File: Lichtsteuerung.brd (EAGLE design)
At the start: 157.7 x 86.4 mm, 136 parts, among them IC1 74HC595D, IC10 TSR_1-2450, IC11 MEGA64-A, IC12 75176AD, IC13 DS1307SO8, IC2 74HC595D, IC3 74HC595D, IC4 74HC595D, IC5 75176AD, IC6 MEGA8-AI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

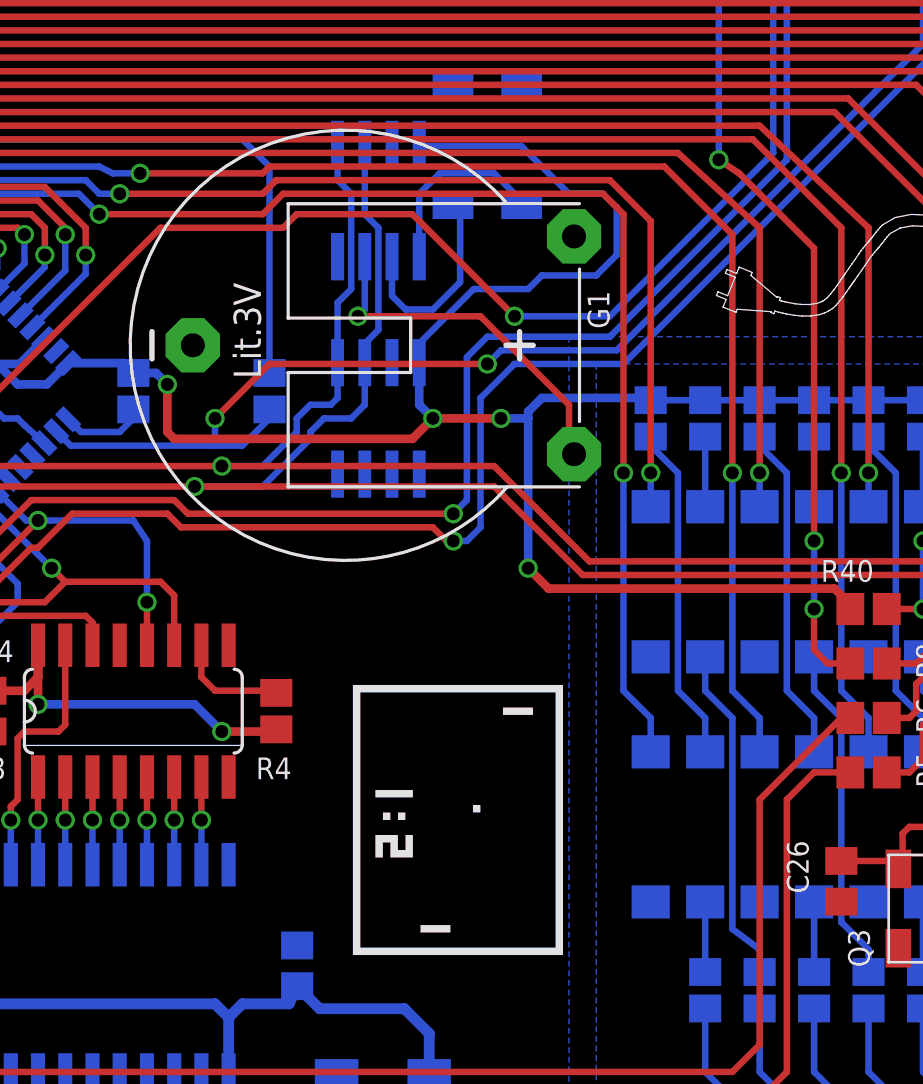
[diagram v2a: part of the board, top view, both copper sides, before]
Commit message: Fixed wrong battery holder
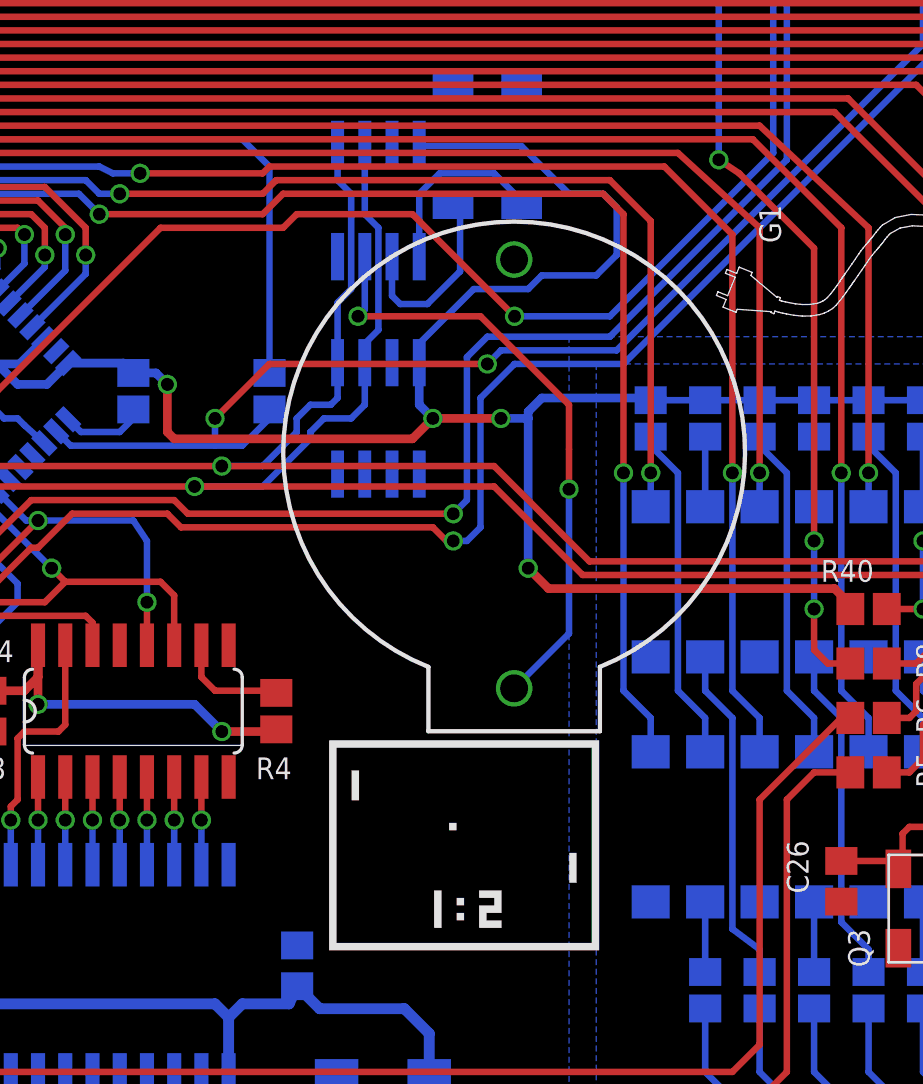
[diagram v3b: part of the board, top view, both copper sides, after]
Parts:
- G1: value CR2032H -> (none); device battery:CR2032H -> SparkFun:BATTCOM_20MM_PTH
- moved G1 8.94 mm to (104.1, 56.9)
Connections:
- net GND: now also G1.2; no longer G1.-
- net N$40: now also G1.1; no longer G1.+
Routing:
- net N$40: track 16.9 -> 28.8 mm, vias 1 -> 2
- net N$42: track 9.51 -> 9.01 mm
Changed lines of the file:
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@@
 <setting verticaltext="up"/>
 </settings>
-<grid distance="39.3700787" unitdist="mil" unit="mil" style="lines" multiple="1" display="yes" altdistance="0.5" altunitdist="mm" altunit="mm"/>
+<grid distance="0.254" unitdist="mm" unit="mm" style="lines" multiple="5" display="yes" altdistance="1.27" altunitdist="mm" altunit="mm"/>
 <layers>
 <layer number="1" name="Top" color="4" fill="1" visible="yes" active="yes"/>
@@
 <text x="7.7" y="4.2" size="1.016" layer="25" rot="R90">Digital Outputs</text>
 <text x="60.9" y="4.2" size="1.016" layer="25" rot="R90">Digital Outputs</text>
-<rectangle x1="100.275" y1="25.025" x2="100.625" y2="26.425" layer="25" rot="R90"/>
-<rectangle x1="104.125" y1="35.175" x2="104.475" y2="36.575" layer="25" rot="R90"/>
-<rectangle x1="102.2" y1="31.15" x2="102.55" y2="31.5" layer="25" rot="R90"/>
-<rectangle x1="97.3" y1="29.4" x2="98.35" y2="29.75" layer="25" rot="R90"/>
-<rectangle x1="98.175" y1="29.575" x2="98.525" y2="30.275" layer="25" rot="R90"/>
-<rectangle x1="98.175" y1="29.225" x2="98.875" y2="29.575" layer="25" rot="R90"/>
-<rectangle x1="98.875" y1="28.875" x2="99.225" y2="29.575" layer="25" rot="R90"/>
-<rectangle x1="98.875" y1="29.575" x2="99.575" y2="29.925" layer="25" rot="R90"/>
-<rectangle x1="98" y1="30.8" x2="98.35" y2="31.15" layer="25" rot="R90"/>
-<rectangle x1="98.7" y1="30.8" x2="99.05" y2="31.15" layer="25" rot="R90"/>
-<rectangle x1="98.35" y1="31.15" x2="98.7" y2="32.9" layer="25" rot="R90"/>
-<rectangle x1="90.825" y1="30.625" x2="102.725" y2="30.975" layer="25" rot="R90"/>
-<rectangle x1="99.925" y1="30.625" x2="112.525" y2="30.975" layer="25" rot="R90"/>
-<rectangle x1="101.15" y1="19.95" x2="101.5" y2="29.4" layer="25" rot="R90"/>
-<rectangle x1="101.15" y1="32.2" x2="101.5" y2="41.65" layer="25" rot="R90"/>
+<rectangle x1="106.688" y1="27.868" x2="107.038" y2="29.268" layer="25" rot="R180"/>
+<rectangle x1="96.538" y1="31.718" x2="96.888" y2="33.118" layer="25" rot="R180"/>
+<rectangle x1="101.088" y1="30.318" x2="101.438" y2="30.668" layer="25" rot="R180"/>
+<rectangle x1="102.488" y1="25.768" x2="103.538" y2="26.118" layer="25" rot="R180"/>
+<rectangle x1="102.488" y1="26.118" x2="102.838" y2="26.818" layer="25" rot="R180"/>
+<rectangle x1="102.838" y1="26.468" x2="103.538" y2="26.818" layer="25" rot="R180"/>
+<rectangle x1="103.188" y1="26.818" x2="103.538" y2="27.518" layer="25" rot="R180"/>
+<rectangle x1="102.488" y1="27.168" x2="103.188" y2="27.518" layer="25" rot="R180"/>
+<rectangle x1="101.438" y1="26.118" x2="101.788" y2="26.468" layer="25" rot="R180"/>
+<rectangle x1="101.438" y1="26.818" x2="101.788" y2="27.168" layer="25" rot="R180"/>
+<rectangle x1="100.388" y1="25.768" x2="100.738" y2="27.518" layer="25" rot="R180"/>
+<rectangle x1="95.838" y1="24.718" x2="107.738" y2="25.068" layer="25" rot="R180"/>
+<rectangle x1="95.488" y1="34.168" x2="108.088" y2="34.518" layer="25" rot="R180"/>
+<rectangle x1="107.738" y1="24.718" x2="108.088" y2="34.168" layer="25" rot="R180"/>
+<rectangle x1="95.488" y1="24.718" x2="95.838" y2="34.168" layer="25" rot="R180"/>
 <rectangle x1="4.2" y1="37.1" x2="5.95" y2="37.45" layer="26"/>
 <rectangle x1="5.95" y1="36.75" x2="6.65" y2="37.1" layer="26"/>
@@
 <attribute name="NAME" x="95.25" y="61.2775" size="1.016" layer="26" rot="MR270"/>
 </element>
-<element name="G1" library="battery" package="CR2032H" value="CR2032H" x="96.12" y="52.94" smashed="yes" rot="R270">
-<attribute name="NAME" x="107.55" y="55.48" size="1.016" layer="25" ratio="10" rot="R270"/>
+<element name="G1" library="SparkFun" package="BATTCOM_20MM_PTH" value="" x="104.12" y="56.94" smashed="yes" rot="R270">
+<attribute name="NAME" x="115.55" y="59.48" size="1.016" layer="25" ratio="10" rot="R270"/>
 </element>
 <element name="Q1" library="crystal" package="MC-306" value="32.768" x="102.87" y="62.23" smashed="yes" rot="MR90">
@@
 <contactref element="C9" pad="2"/>
 <contactref element="C10" pad="2"/>
-<contactref element="G1" pad="-"/>
+<contactref element="G1" pad="2"/>
 <contactref element="IC13" pad="4"/>
 <contactref element="C12" pad="2"/>
@@
 </signal>
 <signal name="N$40">
-<contactref element="G1" pad="+"/>
+<contactref element="G1" pad="1"/>
 <contactref element="IC13" pad="3"/>
 <wire x1="97.155" y1="57.0738" x2="97.155" y2="54.61" width="0.3048" layer="16"/>
@@
 <wire x1="102.5525" y1="54.2925" x2="106.68" y2="50.165" width="0.3048" layer="1"/>
 <wire x1="106.68" y1="50.165" x2="106.68" y2="48.095" width="0.3048" layer="1"/>
-<wire x1="106.68" y1="48.095" x2="106.915" y2="47.86" width="0.3048" layer="1"/>
+<wire x1="106.68" y1="48.095" x2="106.68" y2="46.228" width="0.3048" layer="1"/>
+<via x="106.68" y="46.228" extent="1-16" drill="0.6" shape="square"/>
+<wire x1="106.68" y1="46.228" x2="106.68" y2="39.5" width="0.3048" layer="16"/>
+<wire x1="106.68" y1="39.5" x2="104.12" y2="36.94" width="0.3048" layer="16"/>
 </signal>
 <signal name="SCL">
@@
 <contactref element="Q1" pad="1"/>
 <wire x1="98.425" y1="57.0738" x2="98.425" y2="55.245" width="0.3048" layer="16"/>
-<wire x1="98.425" y1="55.245" x2="99.06" y2="54.61" width="0.3048" layer="16"/>
-<wire x1="99.06" y1="54.61" x2="100.33" y2="54.61" width="0.3048" layer="16"/>
-<wire x1="100.33" y1="54.61" x2="101.6" y2="55.88" width="0.3048" layer="16"/>
-<wire x1="101.6" y1="55.88" x2="101.6" y2="59.0875" width="0.3048" layer="16"/>
+<wire x1="98.425" y1="55.245" x2="98.806" y2="54.864" width="0.3048" layer="16"/>
+<wire x1="98.806" y1="54.864" x2="100.076" y2="54.864" width="0.3048" layer="16"/>
+<wire x1="100.076" y1="54.864" x2="101.6" y2="56.388" width="0.3048" layer="16"/>
+<wire x1="101.6" y1="56.388" x2="101.6" y2="59.0875" width="0.3048" layer="16"/>
 <wire x1="101.6" y1="59.0875" x2="101.27" y2="59.48" width="0.3048" layer="16"/>
 </signal>

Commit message: Added missing bypass cap for the second avr
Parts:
- added C21: 100n, resistor:C0805
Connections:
- net +5V: now also C21.2
- net GND: now also C21.1
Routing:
- net +5V: track 521.2 -> 525.4 mm
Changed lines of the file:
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@@
 <layer number="14" name="Route14" color="1" fill="6" visible="no" active="no"/>
 <layer number="15" name="Route15" color="4" fill="6" visible="no" active="no"/>
-<layer number="16" name="Bottom" color="1" fill="1" visible="yes" active="yes"/>
+<layer number="16" name="Bottom" color="1" fill="1" visible="no" active="yes"/>
 <layer number="17" name="Pads" color="2" fill="1" visible="yes" active="yes"/>
 <layer number="18" name="Vias" color="2" fill="1" visible="yes" active="yes"/>
@@
 <element name="F4" library="ptc-littlefuse" package="1812L" value="500mA" x="98" y="18" rot="MR0"/>
 <element name="F5" library="ptc-littlefuse" package="1812L" value="500mA" x="153" y="15" rot="MR270"/>
+<element name="C21" library="resistor" package="C0805" value="100n" x="135.636" y="42.164" rot="R180"/>
 </elements>
 <signals>
@@
 <via x="59.055" y="43.18" extent="1-16" drill="0.6"/>
 <via x="67.31" y="41.91" extent="1-16" drill="0.6"/>
+<contactref element="C21" pad="1"/>
 </signal>
 <signal name="N$36">
@@
 <wire x1="137.16" y1="82.55" x2="135.89" y2="81.28" width="0.3048" layer="16"/>
 <wire x1="135.89" y1="81.28" x2="135.89" y2="80.01" width="0.3048" layer="16"/>
+<contactref element="C21" pad="2"/>
+<wire x1="134.32816875" y1="38.67248125" x2="134.43048125" y2="38.67248125" width="0.3048" layer="1"/>
+<wire x1="134.43048125" y1="38.67248125" x2="135.382" y2="39.624" width="0.3048" layer="1"/>
+<wire x1="135.382" y1="39.624" x2="135.382" y2="40.386" width="0.3048" layer="1"/>
+<wire x1="135.382" y1="40.386" x2="134.874" y2="40.894" width="0.3048" layer="1"/>
+<wire x1="134.874" y1="40.894" x2="134.874" y2="42.076" width="0.3048" layer="1"/>
+<wire x1="134.874" y1="42.076" x2="134.786" y2="42.164" width="0.3048" layer="1"/>
 </signal>
 <signal name="SR_SCK">

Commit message: Fixed serial eeprom footprint
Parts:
- IC9: device microchip:SO-08 -> microchip:SO-08M
- moved IC9 0.76 mm to (97.8, 48.8)
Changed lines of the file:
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@@
 <grid distance="0.254" unitdist="mm" unit="mm" style="lines" multiple="5" display="yes" altdistance="1.27" altunitdist="mm" altunit="mm"/>
 <layers>
-<layer number="1" name="Top" color="4" fill="1" visible="yes" active="yes"/>
+<layer number="1" name="Top" color="4" fill="1" visible="no" active="yes"/>
 <layer number="2" name="Route2" color="1" fill="3" visible="no" active="no"/>
 <layer number="3" name="Route3" color="4" fill="3" visible="no" active="no"/>
@@
 <layer number="14" name="Route14" color="1" fill="6" visible="no" active="no"/>
 <layer number="15" name="Route15" color="4" fill="6" visible="no" active="no"/>
-<layer number="16" name="Bottom" color="1" fill="1" visible="no" active="yes"/>
+<layer number="16" name="Bottom" color="1" fill="1" visible="yes" active="yes"/>
 <layer number="17" name="Pads" color="2" fill="1" visible="yes" active="yes"/>
 <layer number="18" name="Vias" color="2" fill="1" visible="yes" active="yes"/>
@@
 <attribute name="NAME" x="70.866" y="37.6555" size="1.016" layer="26" rot="MR90"/>
 </element>
-<element name="IC9" library="microchip" package="SO-08" value="24FC128-I/SN" x="97.79" y="49.53" smashed="yes" rot="MR0">
-<attribute name="MF" value="" x="97.79" y="49.53" size="1.778" layer="28" rot="MR0" display="off"/>
-<attribute name="MPN" value="24AA256T-I/SM" x="97.79" y="49.53" size="1.778" layer="28" rot="MR0" display="off"/>
-<attribute name="OC_FARNELL" value="1579570" x="97.79" y="49.53" size="1.778" layer="28" rot="MR0" display="off"/>
-<attribute name="OC_NEWARK" value="08N6838" x="97.79" y="49.53" size="1.778" layer="28" rot="MR0" display="off"/>
-<attribute name="NAME" x="100.457" y="48.26" size="1.016" layer="26" rot="MR90"/>
+<element name="IC9" library="microchip" package="SO-08M" value="24FC128-I/SN" x="97.79" y="48.768" smashed="yes" rot="MR0">
+<attribute name="MF" value="MICROCHIP" x="97.79" y="48.768" size="1.778" layer="28" rot="MR0" display="off"/>
+<attribute name="MPN" value="24AA01-I/SN" x="97.79" y="48.768" size="1.778" layer="28" rot="MR0" display="off"/>
+<attribute name="OC_FARNELL" value="1331268" x="97.79" y="48.768" size="1.778" layer="28" rot="MR0" display="off"/>
+<attribute name="OC_NEWARK" value="92C6793" x="97.79" y="48.768" size="1.778" layer="28" rot="MR0" display="off"/>
+<attribute name="NAME" x="100.457" y="47.498" size="1.016" layer="26" rot="MR90"/>
 </element>
 <element name="IC10" library="_traco_tsr-1" package="TSR-1" value="TSR_1-2450" x="41.91" y="60.96" smashed="yes" rot="R180">
@@
 <wire x1="105.41" y1="50.4825" x2="110.3875" y2="50.4825" width="0.4064" layer="16"/>
 <wire x1="110.3875" y1="50.4825" x2="110.49" y2="50.38" width="0.4064" layer="16"/>
-<wire x1="99.695" y1="52.13" x2="99.695" y2="50.165" width="0.4064" layer="16"/>
+<wire x1="99.695" y1="52.098" x2="99.695" y2="50.165" width="0.4064" layer="16"/>
 <wire x1="99.695" y1="50.165" x2="100.33" y2="49.53" width="0.4064" layer="16"/>
 <via x="100.33" y="49.53" extent="1-16" drill="0.6"/>
@@
 <wire x1="62.865" y1="37.1475" x2="62.5475" y2="36.83" width="0.3048" layer="1"/>
 <wire x1="62.5475" y1="36.83" x2="62.5475" y2="35.45" width="0.3048" layer="1"/>
-<wire x1="99.695" y1="52.13" x2="99.695" y2="53.0225" width="0.3048" layer="16"/>
+<wire x1="99.695" y1="52.098" x2="99.695" y2="53.0225" width="0.3048" layer="16"/>
 <wire x1="99.695" y1="53.0225" x2="102.235" y2="55.5625" width="0.3048" layer="16"/>
 <wire x1="102.235" y1="55.5625" x2="104.775" y2="55.5625" width="0.3048" layer="16"/>
@@
 <wire x1="97.79" y1="58.42" x2="97.79" y2="53.6575" width="0.3048" layer="16"/>
 <wire x1="97.79" y1="53.6575" x2="97.155" y2="53.0225" width="0.3048" layer="16"/>
-<wire x1="97.155" y1="53.0225" x2="97.155" y2="52.13" width="0.3048" layer="16"/>
+<wire x1="97.155" y1="53.0225" x2="97.155" y2="52.098" width="0.3048" layer="16"/>
 <wire x1="67.894678125" y1="45.59145" x2="67.894678125" y2="45.669678125" width="0.3048" layer="16"/>
 <wire x1="67.894678125" y1="45.669678125" x2="69.5325" y2="47.3075" width="0.3048" layer="16"/>
@@
 <via x="61.2775" y="53.6575" extent="1-16" drill="0.6"/>
 <wire x1="61.2775" y1="53.6575" x2="61.9125" y2="53.0225" width="0.3048" layer="1"/>
-<wire x1="97.155" y1="52.13" x2="97.155" y2="50.165" width="0.3048" layer="16"/>
+<wire x1="97.155" y1="52.098" x2="97.155" y2="50.165" width="0.3048" layer="16"/>
 <wire x1="97.155" y1="50.165" x2="96.52" y2="49.53" width="0.3048" layer="16"/>
 <wire x1="96.52" y1="49.53" x2="95.25" y2="49.53" width="0.3048" layer="16"/>
@@
 <contactref element="IC6" pad="27"/>
 <contactref element="X7" pad="L2"/>
-<wire x1="95.885" y1="52.13" x2="95.885" y2="54.9275" width="0.3048" layer="16"/>
+<wire x1="95.885" y1="52.098" x2="95.885" y2="54.9275" width="0.3048" layer="16"/>
 <wire x1="95.885" y1="54.9275" x2="96.52" y2="55.5625" width="0.3048" layer="16"/>
 <wire x1="96.52" y1="55.5625" x2="96.52" y2="60.0075" width="0.3048" layer="16"/>
@@
 <wire x1="58.1025" y1="54.9275" x2="61.2775" y2="52.3875" width="0.3048" layer="16"/>
 <via x="61.2775" y="52.3875" extent="1-16" drill="0.6"/>
-<wire x1="95.885" y1="52.13" x2="95.885" y2="50.4825" width="0.3048" layer="16"/>
+<wire x1="95.885" y1="52.098" x2="95.885" y2="50.4825" width="0.3048" layer="16"/>
 <wire x1="95.885" y1="50.4825" x2="95.5675" y2="50.165" width="0.3048" layer="16"/>
 <wire x1="95.5675" y1="50.165" x2="94.615" y2="50.165" width="0.3048" layer="16"/>
